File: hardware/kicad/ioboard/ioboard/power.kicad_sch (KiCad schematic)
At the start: 30 parts, among them J1 PWR_IN, Q1 CSD18531Q5A, U1 LM74610QDGKRQ1, U2 TVS3300DRV, U3 171013801, U4 171013801, U5 171033801, U6 R1SX-3.33.3-R

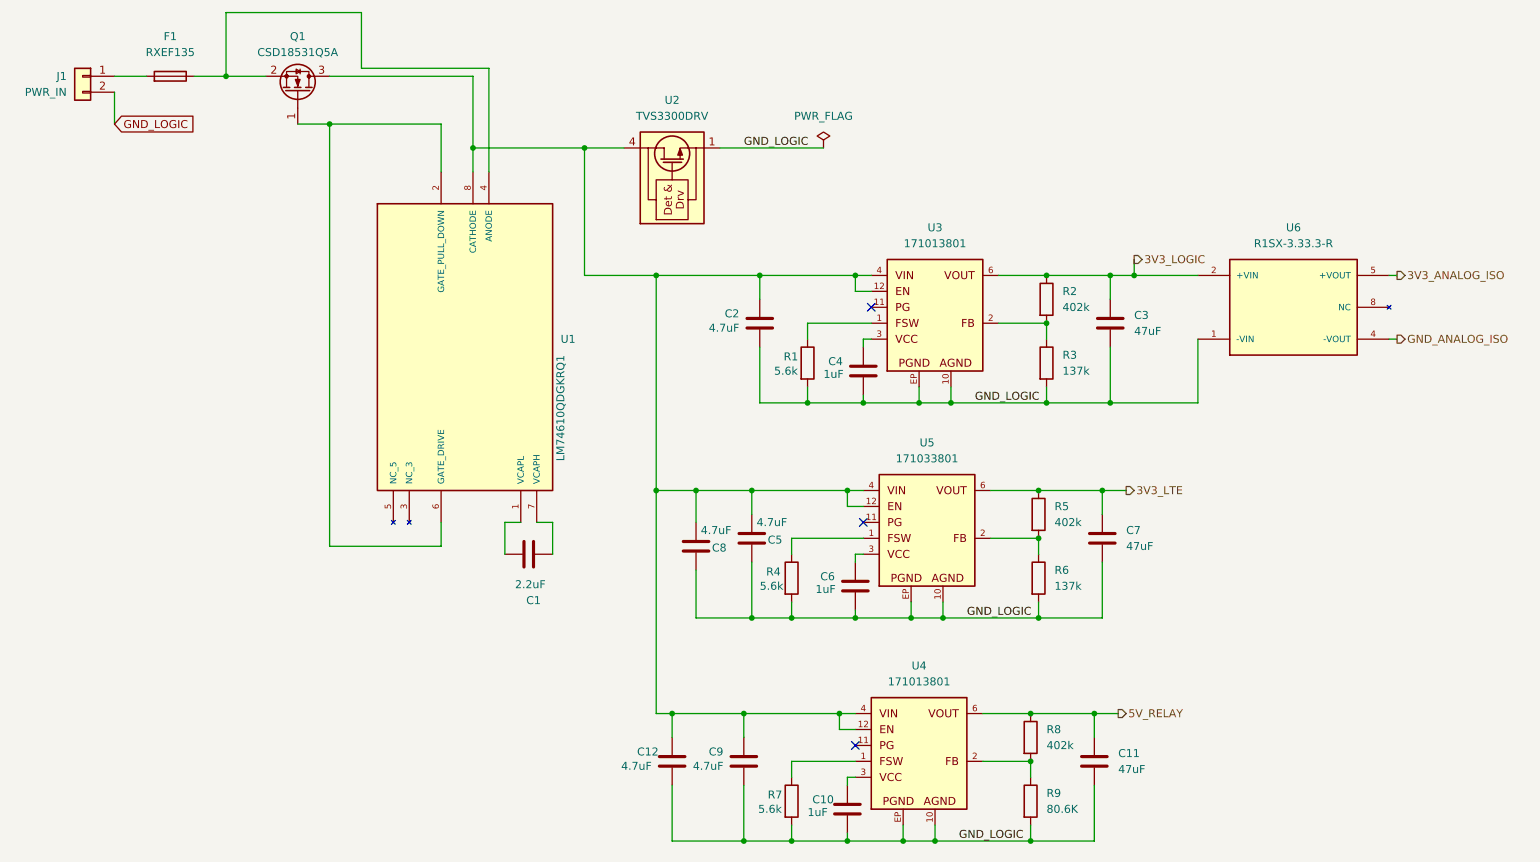
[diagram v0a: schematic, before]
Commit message: analog-io: ERC clean, Steps 6-9 closed, subsystem complete
KiCad ERC run on analog_io.kicad_sch (plus the directly-tied root-sheet
pin) to a fully-explained clean state: 15 findings reviewed and excluded
with a written, per-violation comment (cross-sheet power-driver false
positives, documented spare/deferred headroom, deferred GPIO assignment,
the deferred 15V_ANALOG_ISO rail) -- nothing silently suppressed.

Two real, pre-existing bugs outside this sheet were caught and fixed
along the way, both recorded in power.md's own revision history:
- Duplicate reference collision: power.kicad_sch's reverse-polarity FET
  was also Q1, colliding with relay_outputs.kicad_sch's Q1-Q4. Renamed
  to Q5 (schematic, power_bom.csv, and every prose reference in power.md
  updated to match).
- Inconsistent GND_LOGIC labeling: power.kicad_sch had one global label
  plus four stray local labels for the same net. All four converted to
  global.

Bare R_in/R_f renamed to R_in1/R_f1 by KiCad's own Annotate tool.

Steps 7 (acceptance criteria), 8 (documentation & BOM -- new
hardware/bom/analog_io_bom.csv), and 9 (sign-off) closed out. All 9
steps of this subsystem's build plan are now done.

Co-Authored-By: Claude Sonnet 5 <noreply@anthropic.com>
Claude-Session: https://claude.ai/code/session_011Mk4ACKLUzGL8p2SUjrweQ
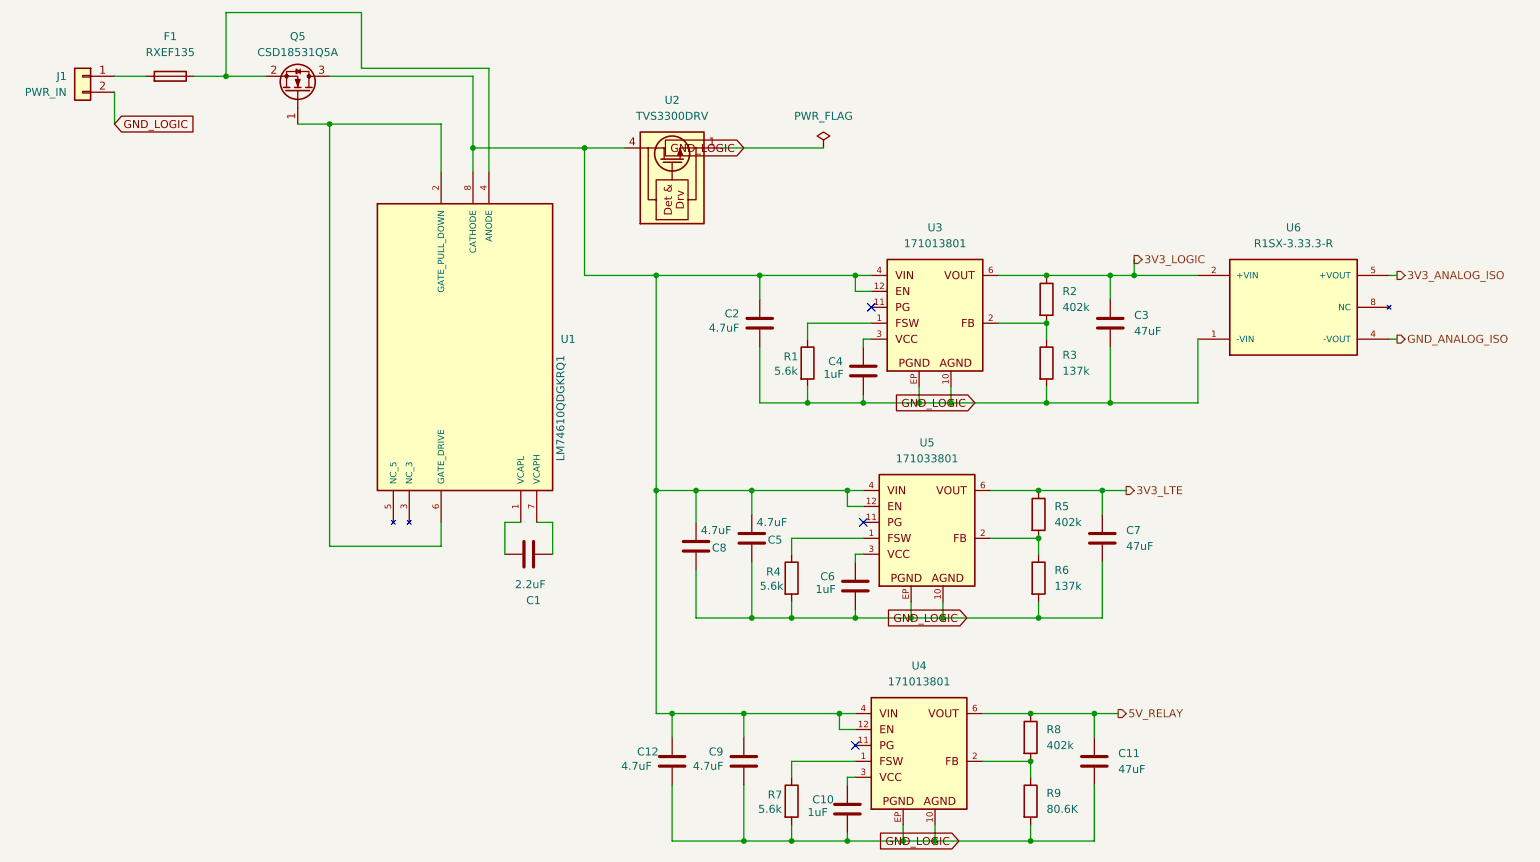
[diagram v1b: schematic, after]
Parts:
- renumbered Q1 to Q5
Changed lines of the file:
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@@
 		)
 	)
-	(label "GND_LOGIC"
-		(at 138.43 45.72 0)
+	(global_label "GND_LOGIC"
+		(shape input)
+		(at 173.99 120.65 180)
+		(fields_autoplaced yes)
 		(effects
 			(font
 				(size 1.27 1.27)
 			)
-			(justify left bottom)
-		)
-	)
-	(label "GND_LOGIC"
-		(at 173.99 120.65 0)
-		(effects
-			(font
-				(size 1.27 1.27)
-			)
-			(justify left bottom)
-		)
-	)
-	(label "GND_LOGIC"
-		(at 175.26 86.36 0)
-		(effects
-			(font
-				(size 1.27 1.27)
-			)
-			(justify left bottom)
-		)
-	)
-	(label "GND_LOGIC"
-		(at 172.72 156.21 0)
-		(effects
-			(font
-				(size 1.27 1.27)
-			)
-			(justify left bottom)
+			(justify right)
+		)
+		(property "Intersheetrefs" "${INTERSHEET_REFS}"
+			(at 160.6633 120.65 0)
+			(effects
+				(font
+					(size 1.27 1.27)
+				)
+				(justify right)
+				(hide yes)
+			)
 		)
 	)
@@
 				)
 				(justify left)
+				(hide yes)
+			)
+		)
+	)
+	(global_label "GND_LOGIC"
+		(shape input)
+		(at 175.26 86.36 180)
+		(fields_autoplaced yes)
+		(effects
+			(font
+				(size 1.27 1.27)
+			)
+			(justify right)
+		)
+		(property "Intersheetrefs" "${INTERSHEET_REFS}"
+			(at 161.9333 86.36 0)
+			(effects
+				(font
+					(size 1.27 1.27)
+				)
+				(justify right)
+				(hide yes)
+			)
+		)
+	)
+	(global_label "GND_LOGIC"
+		(shape input)
+		(at 172.72 156.21 180)
+		(fields_autoplaced yes)
+		(effects
+			(font
+				(size 1.27 1.27)
+			)
+			(justify right)
+		)
+		(property "Intersheetrefs" "${INTERSHEET_REFS}"
+			(at 159.3933 156.21 0)
+			(effects
+				(font
+					(size 1.27 1.27)
+				)
+				(justify right)
+				(hide yes)
+			)
+		)
+	)
+	(global_label "GND_LOGIC"
+		(shape input)
+		(at 138.43 45.72 180)
+		(fields_autoplaced yes)
+		(effects
+			(font
+				(size 1.27 1.27)
+			)
+			(justify right)
+		)
+		(property "Intersheetrefs" "${INTERSHEET_REFS}"
+			(at 125.1033 45.72 0)
+			(effects
+				(font
+					(size 1.27 1.27)
+				)
+				(justify right)
 				(hide yes)
 			)
@@
 		(on_board yes)
 		(dnp no)
-		(property "Reference" "Q1"
+		(property "Reference" "Q5"
 			(at 67.31 27.94 90)
 			(effects
@@
 			(project ""
 				(path "/a0fa9f92-ef51-408b-9617-1545f9e9dad8/9bc843cc-645c-4034-a877-ed0cc8bfa13d"
-					(reference "Q1")
+					(reference "Q5")
 					(unit 1)
 				)
